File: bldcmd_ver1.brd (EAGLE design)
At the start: 43 x 43 mm, 88 parts, among them CN1 DF61-2P-2.2V(23), CN2 DF65-3P-1.7V(21), CN3 DF57H-5P-1.2V(21), CN5 SM04B-SRSS-TB, CN6 SM05B-SRSS-TB, CN7 SM04B-SRSS-TB, IC1 STSPIN32F0A, IC2 AS5047P-ATSM, IC4 LTC485S, Q1 PSMN2R4-30MLD, Q2 PSMN2R4-30MLD, Q3 PSMN2R4-30MLD, Q4 PSMN2R4-30MLD, Q5 PSMN2R4-30MLD, Q6 PSMN2R4-30MLD, SW1 SKRP

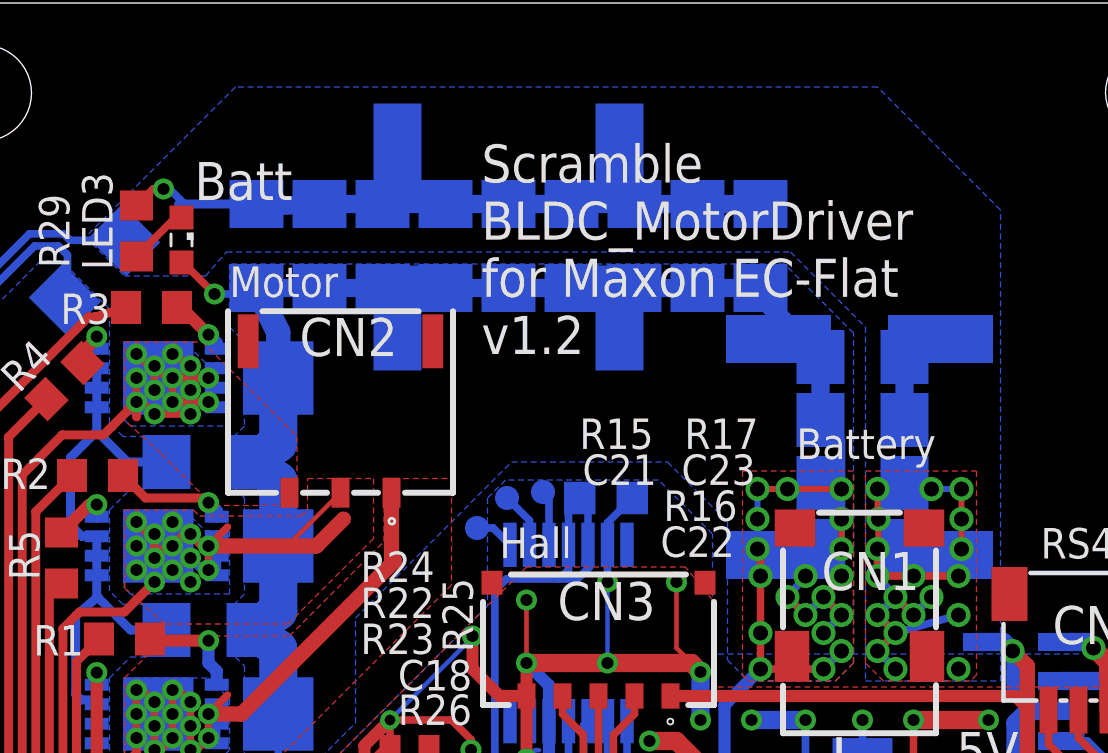
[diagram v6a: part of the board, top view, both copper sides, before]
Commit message: 電源ラインのセラミックコンデンサ削除
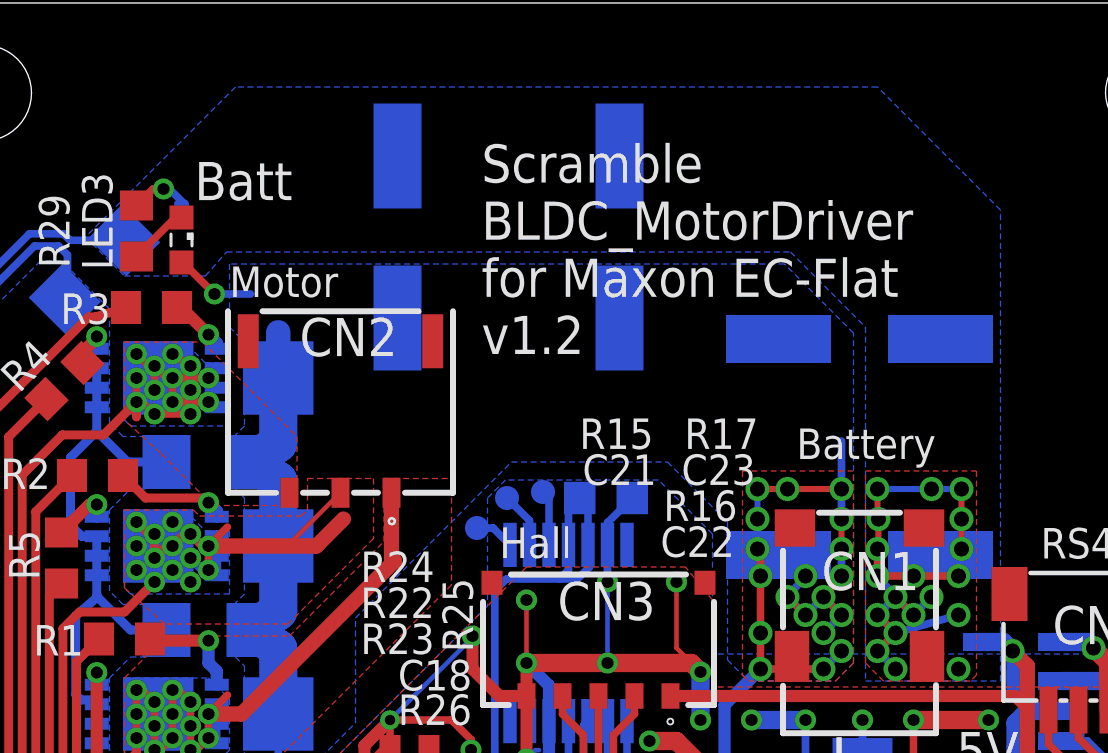
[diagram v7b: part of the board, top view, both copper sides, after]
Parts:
- removed C14, C15, C16, C24, C25, C26, C27, C28, C29, C30, C31, C32, C33: 10u, rcl:C3216
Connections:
- net +12V: no longer C14.1, C15.1, C16.1, C24.2, C25.2, C26.2, C27.2, C28.2, C29.1, C30.1, C31.1, C32.2, C33.1
- net GND: no longer C14.2, C15.2, C16.2, C24.1, C25.1, C26.1, C27.1, C28.1, C29.2, C30.2, C31.2, C32.1, C33.2
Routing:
- net +12V: track 91.0 -> 66.1 mm
- net GND: track 346.1 -> 324.7 mm
